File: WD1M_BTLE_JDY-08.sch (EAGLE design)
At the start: 9 parts, among them J1 CON_HEADER_1X04, Q1 NOFIT_SI2319CDS-T1-GE3

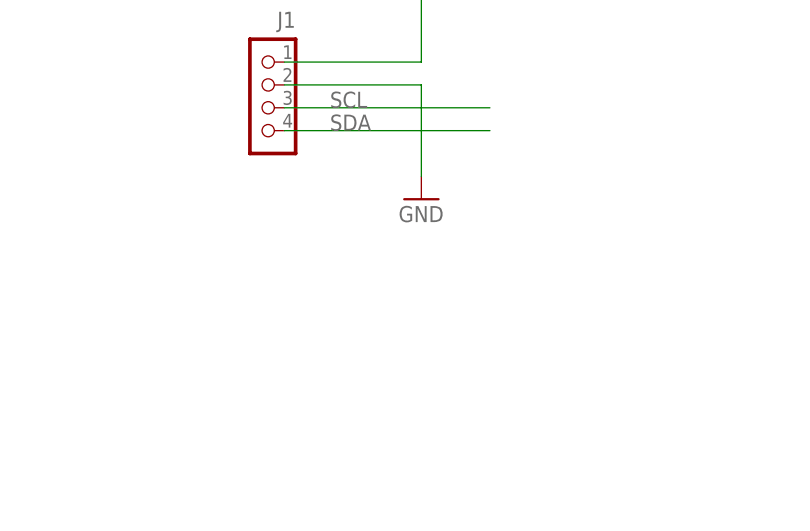
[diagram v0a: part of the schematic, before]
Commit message: Resistor value update
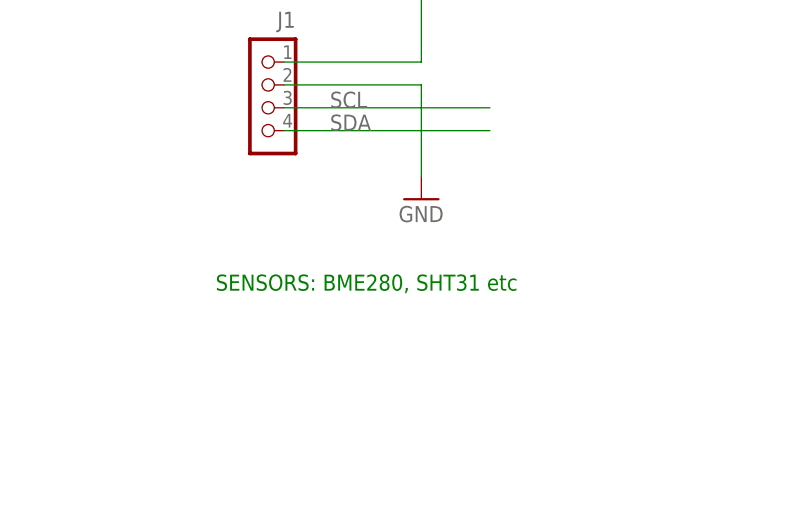
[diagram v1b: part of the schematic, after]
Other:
- note added: "SENSORS: BME280, SHT31 etc"
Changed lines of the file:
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@@
 <text x="83.82" y="45.72" size="1.778" layer="91">LOW = ON
 HIGH = OFF</text>
+<text x="175.26" y="30.48" size="1.778" layer="91">SENSORS: BME280, SHT31 etc</text>
 </plain>
 <instances>
